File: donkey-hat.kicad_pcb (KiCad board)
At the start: 4 copper layers, 65 x 56.5 mm, 62 parts, among them J1 5V, J10 8, J11 9, J12 10, J13 11, J14 NEOPIXEL, J15 MPU-9250, J16 4, J17 5, J18 6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

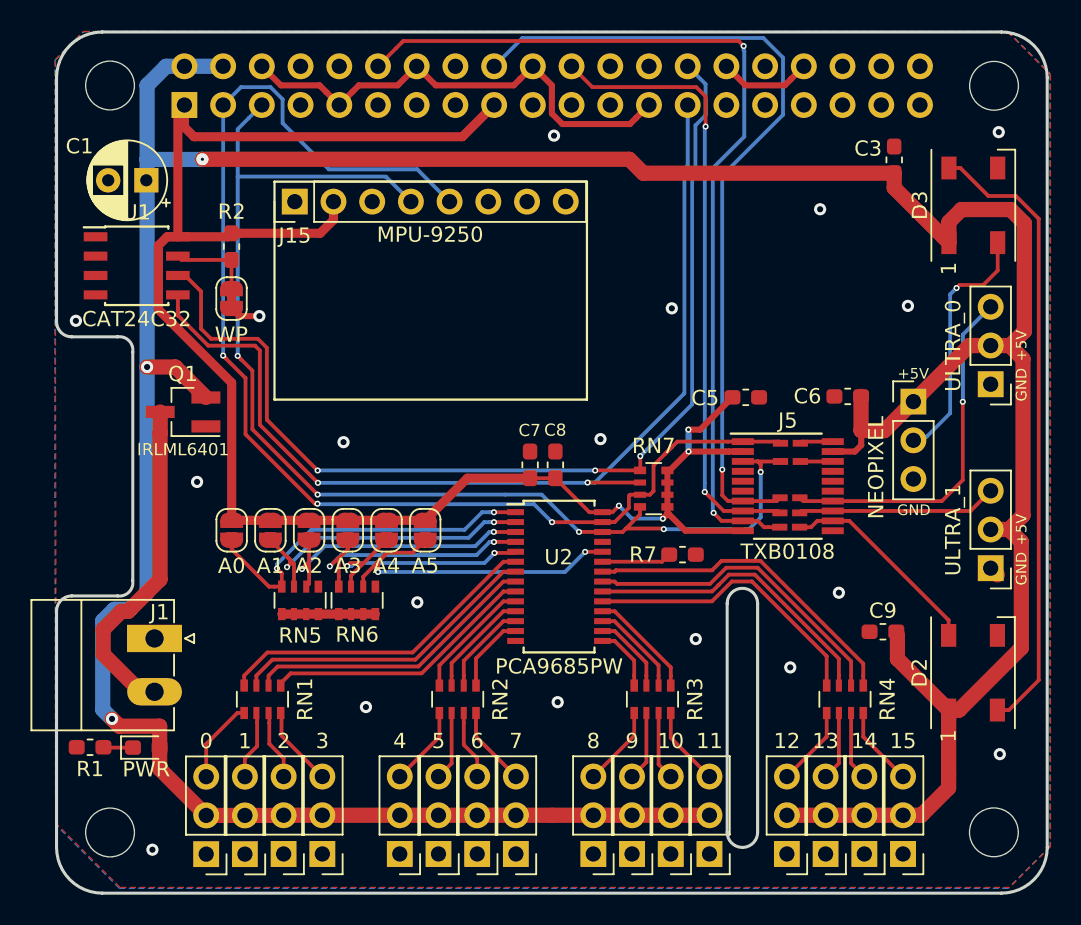
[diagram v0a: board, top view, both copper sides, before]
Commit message: Added logo and text.
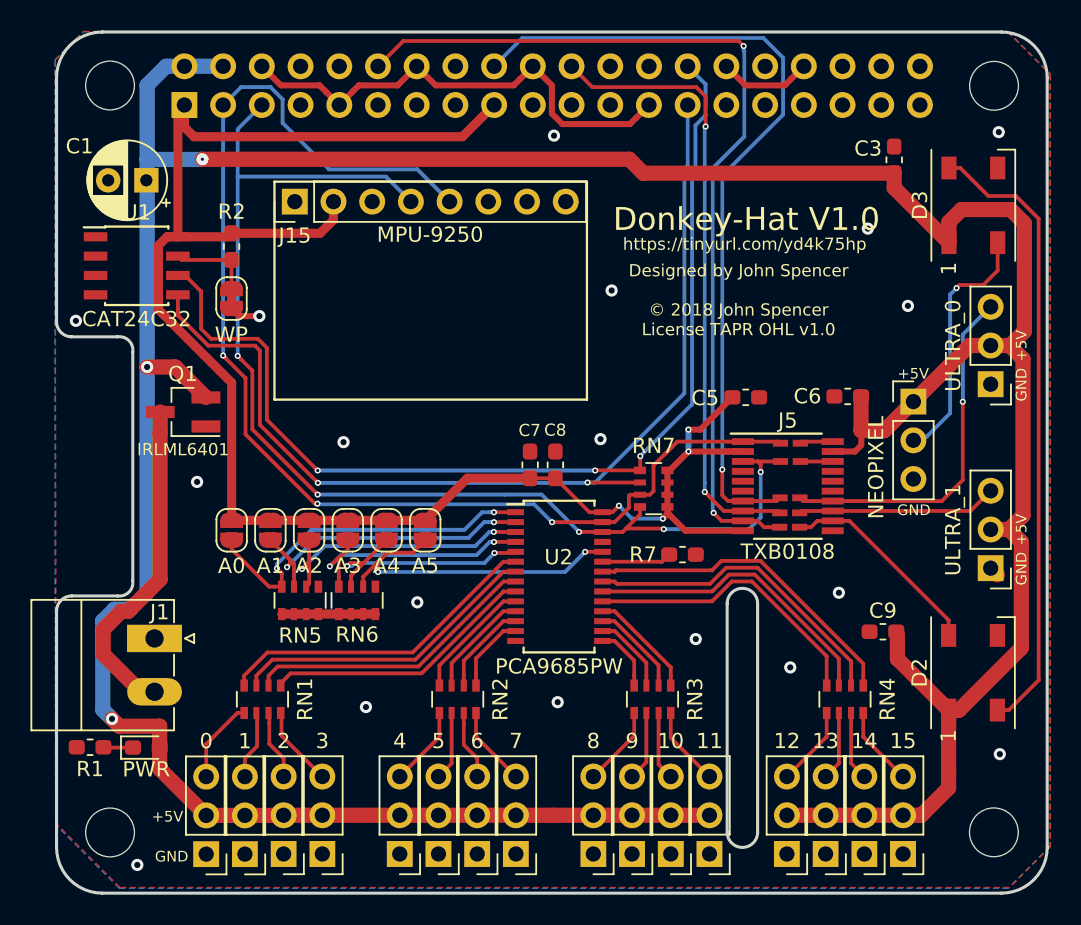
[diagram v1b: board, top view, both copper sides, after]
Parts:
- added G***: LOGO, libs:logo.HeartOfPluto, B.Cu at (91.5, 84.6)
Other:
- board text added: "Designed by John Spencer © 2018 John Spencer License TAPR OHL v1.0"
- board text added: "Donkey-Hat V1.0"
- board text added: "https://tinyurl.com/yd4k75hp"

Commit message: Schematic updated
PWM pins reduced.
level shifter removed.
Ultrasonic model changed.
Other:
- copper layers 4 -> 2
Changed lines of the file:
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@@
   (layers
     (0 F.Cu signal)
-    (1 In1.Cu signal)
-    (2 In2.Cu signal)
     (31 B.Cu signal)
     (32 B.Adhes user)
@@
     (40 Dwgs.User user)
     (41 Cmts.User user)
-    (42 Eco1.User user hide)
-    (43 Eco2.User user hide)
+    (42 Eco1.User user)
+    (43 Eco2.User user)
     (44 Edge.Cuts user)
     (45 Margin user)

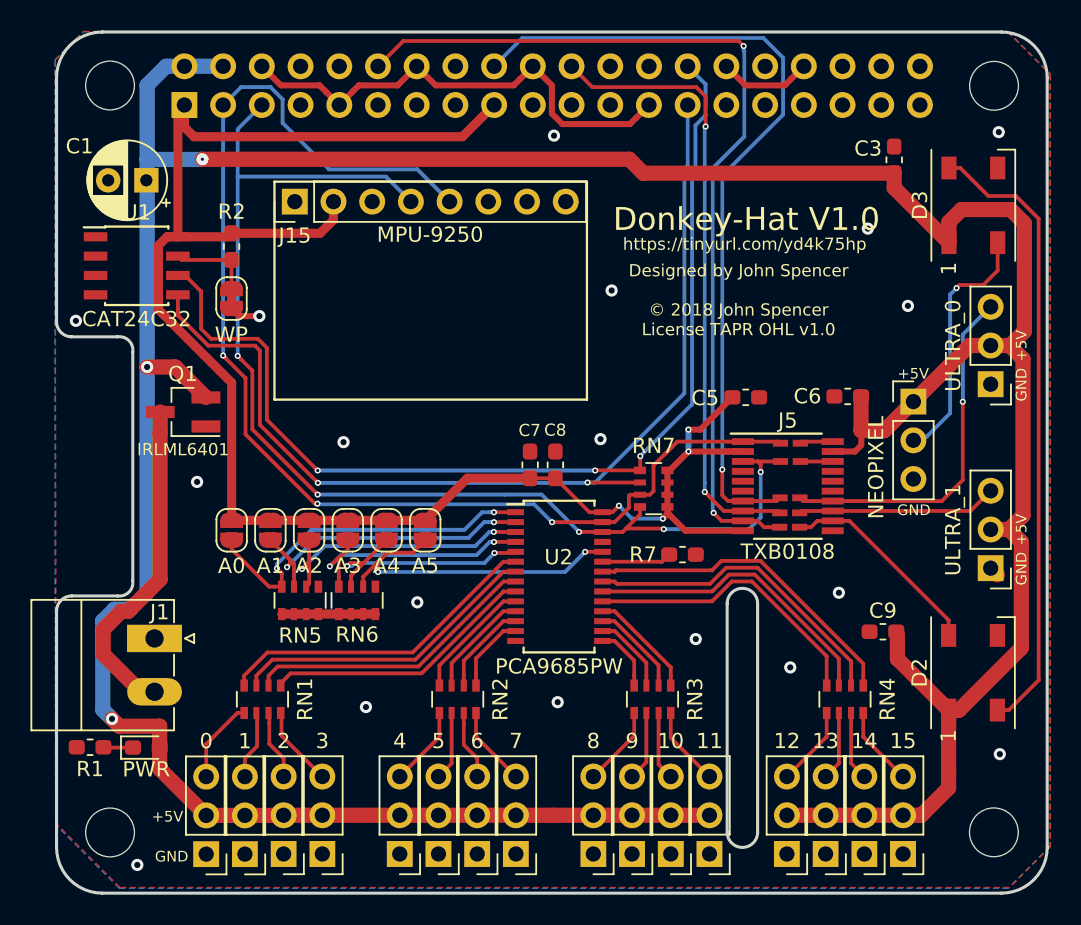
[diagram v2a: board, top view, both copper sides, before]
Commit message: New PCB to take in to account schematic changes
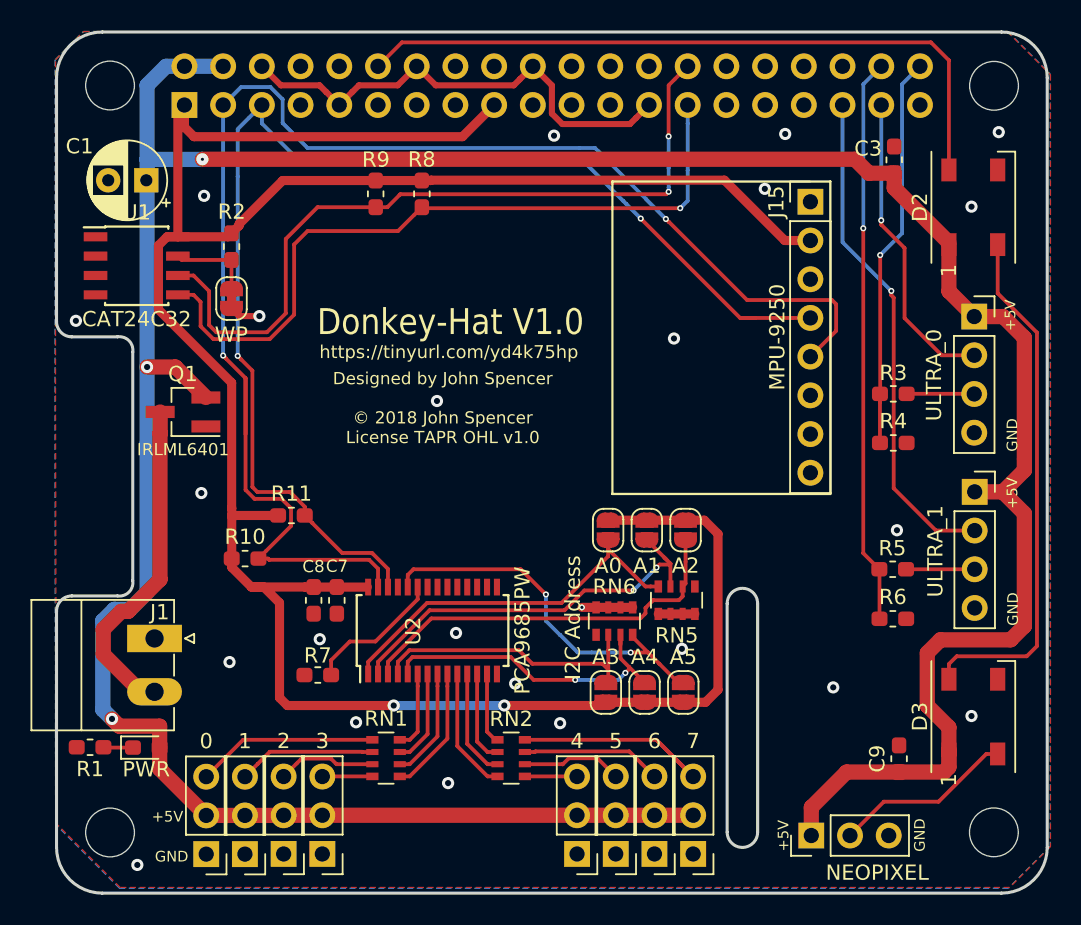
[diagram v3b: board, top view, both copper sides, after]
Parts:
- removed C5, C6: 100nF, Capacitor_SMD:C_0603_1608Metric_Pad1.05x0.95mm_HandSolder
- removed J10: 8, Connector_PinHeader_2.54mm:PinHeader_1x03_P2.54mm_Vertical
- removed J11: 9, Connector_PinHeader_2.54mm:PinHeader_1x03_P2.54mm_Vertical
- removed J12: 10, Connector_PinHeader_2.54mm:PinHeader_1x03_P2.54mm_Vertical
- removed J13: 11, Connector_PinHeader_2.54mm:PinHeader_1x03_P2.54mm_Vertical
- removed J20: 12, Connector_PinHeader_2.54mm:PinHeader_1x03_P2.54mm_Vertical
- removed J21: 13, Connector_PinHeader_2.54mm:PinHeader_1x03_P2.54mm_Vertical
- removed J22: 14, Connector_PinHeader_2.54mm:PinHeader_1x03_P2.54mm_Vertical
- removed J23: 15, Connector_PinHeader_2.54mm:PinHeader_1x03_P2.54mm_Vertical
- removed J5: TXB0108, Package_SO:TSSOP-20_4.4x6.5mm_P0.65mm
- removed JP11, JP12, JP13, JP8, JP9: LINK, libs:SolderJumper-2_small
- removed RN3, RN4: 220_Pack04, Resistor_SMD:R_Array_Convex_4x0603
- removed RN7: 3.9K_Pack04, Resistor_SMD:R_Array_Convex_4x0603
- added R10: 3.9K, Resistor_SMD:R_0603_1608Metric_Pad1.05x0.95mm_HandSolder, F.Cu at (90.9, 95.3)
- added R11: 3.9K, Resistor_SMD:R_0603_1608Metric_Pad1.05x0.95mm_HandSolder, F.Cu at (93.9, 92.5)
- added R3: 330, Resistor_SMD:R_0603_1608Metric_Pad1.05x0.95mm_HandSolder, F.Cu at (133.4, 84.5)
- added R4: 470, Resistor_SMD:R_0603_1608Metric_Pad1.05x0.95mm_HandSolder, F.Cu at (133.4, 87.8)
- added R5: 330, Resistor_SMD:R_0603_1608Metric_Pad1.05x0.95mm_HandSolder, F.Cu at (133.4, 96.0)
- added R6: 470, Resistor_SMD:R_0603_1608Metric_Pad1.05x0.95mm_HandSolder, F.Cu at (133.4, 99.3)
- added R8: 3.9K, Resistor_SMD:R_0603_1608Metric_Pad1.05x0.95mm_HandSolder, F.Cu at (102.5, 71.4)
- added R9: 3.9K, Resistor_SMD:R_0603_1608Metric_Pad1.05x0.95mm_HandSolder, F.Cu at (99.5, 71.4)
- C9: value 1uF -> 100nF
- J3, J4: footprint Connector_PinHeader_2.54mm:PinHeader_1x03_P2.54mm_Vertical -> Connector_PinSocket_2.54mm:PinSocket_1x04_P2.54mm_Vertical
- JP5: value A3 -> A5
- JP7: value A5 -> A3
- moved J15 33.8 mm to (128.0, 71.9), turned to 0 degrees
- moved D3 33.5 mm to (138.7, 105.7)
- moved D2 30.5 mm to (138.7, 72.3)
- moved J14 29.2 mm to (128.1, 113.5), turned to 90 degrees
- moved R7 25.2 mm to (95.7, 103.0), turned to 180 degrees
- moved JP2 24.7 mm to (114.7, 93.5)
- moved JP3 24.7 mm to (117.3, 93.5)
- moved JP4 24.7 mm to (119.8, 93.5)
- moved RN5 24.7 mm to (119.2, 98.1)
- moved JP5 24.4 mm to (119.7, 104.1), turned to 90 degrees
- moved JP6 20.0 mm to (117.1, 104.1), turned to 90 degrees
- moved C8 18.2 mm to (95.4, 98.1), turned to 270 degrees
- moved RN6 16.9 mm to (115.1, 99.5), turned to 90 degrees
- moved JP7 15.9 mm to (114.6, 104.1), turned to 90 degrees
- moved C7 15.5 mm to (96.9, 98.1), turned to 270 degrees
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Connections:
- D2 pad 4: /GPIO18_5 -> /GPIO18
- J3 pad 1: GND -> +5V
- J3 pad 2: +5V -> /GPIO26
- J3 pad 3: /GPIO24_5 -> Net-(J3-Pad3)
- J4 pad 1: GND -> +5V
- J4 pad 2: +5V -> /GPIO19
- J4 pad 3: /GPIO25_5 -> Net-(J4-Pad3)
- JP5 pad 2: /A3 -> /A5
- JP7 pad 2: /A5 -> /A3
- RN6 pad 2: /A5 -> /A3
- RN6 pad 4: /A3 -> /A5
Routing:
- net /GPIO24: track 54.7 -> 0.00 mm, vias 1 -> 0
- net +3V3: track 115.6 -> 169.7 mm, vias 4 -> 2
- net /GPIO25: track 41.1 -> 0.00 mm, vias 2 -> 0
- net /GPIO20: track 0.00 -> 37.2 mm, vias 0 -> 1
- net /GPIO19: track 0.00 -> 33.0 mm, vias 0 -> 1
- net +5V: track 237.1 -> 210.3 mm
- net /GPIO21: track 0.00 -> 25.8 mm, vias 0 -> 1
- net /GPIO24_5: track 23.5 -> 0.00 mm, vias 1 -> 0
- net /PWM15: track 21.8 -> 0.00 mm
- net /PWM14: track 21.0 -> 0.00 mm
- net /GPIO26: track 0.00 -> 20.2 mm, vias 0 -> 1
- net /PWM13: track 20.0 -> 0.00 mm
- net /PWM12: track 19.2 -> 0.00 mm
- net /EEDATA: track 67.0 -> 48.4 mm, vias 2 -> 1
- net /EECLK: track 68.6 -> 50.5 mm, vias 3 -> 2
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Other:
- board text added: "I2C Address"

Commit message: Added 5v regulator
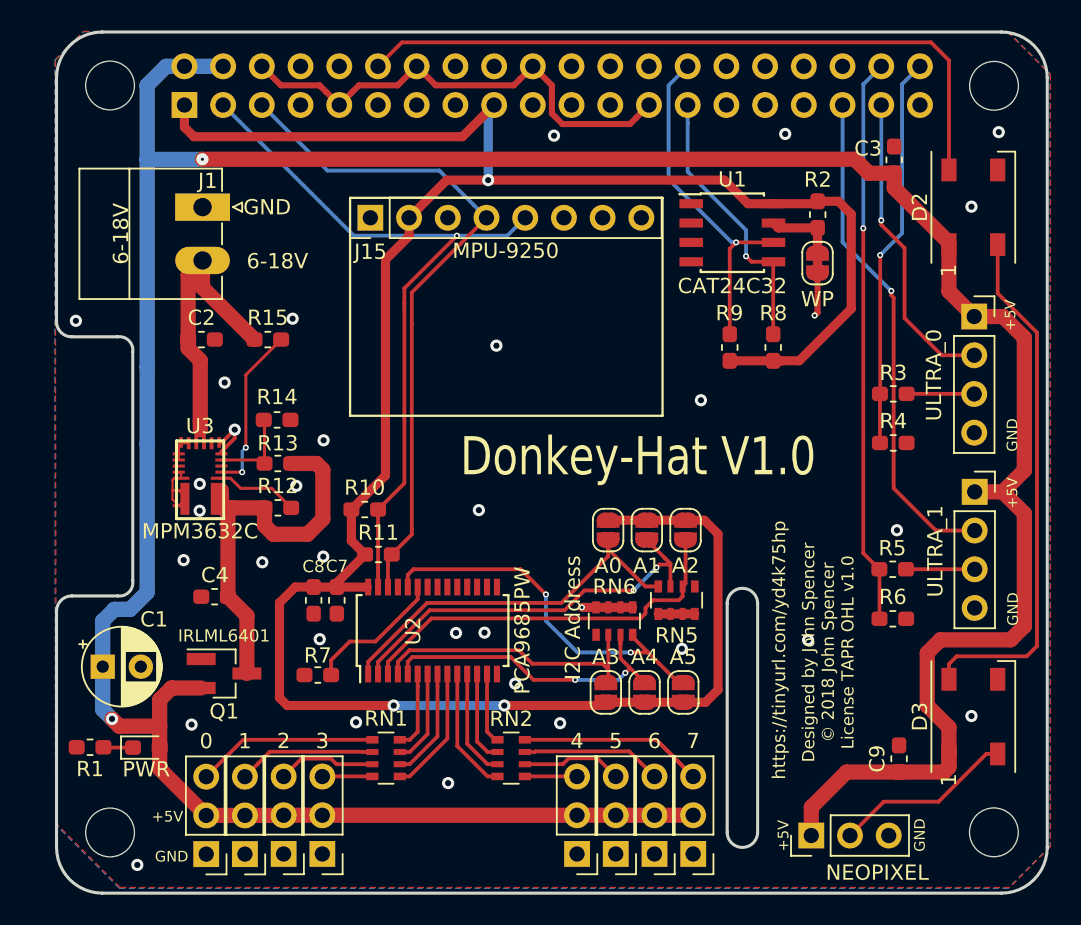
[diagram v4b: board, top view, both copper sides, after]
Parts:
- added C2: 10uF, Capacitor_SMD:C_0603_1608Metric_Pad1.05x0.95mm_HandSolder, F.Cu at (88.0, 81.0)
- added C4: 22uF, Capacitor_SMD:C_0603_1608Metric_Pad1.05x0.95mm_HandSolder, F.Cu at (88.9, 97.8)
- added R12: 1K, Resistor_SMD:R_0603_1608Metric_Pad1.05x0.95mm_HandSolder, F.Cu at (93.0, 92.0)
- added R13: 47K, Resistor_SMD:R_0603_1608Metric_Pad1.05x0.95mm_HandSolder, F.Cu at (93.0, 89.1)
- added R14: 8.87K, Resistor_SMD:R_0603_1608Metric_Pad1.05x0.95mm_HandSolder, F.Cu at (93.0, 86.2)
- added R15: 100K, Resistor_SMD:R_0603_1608Metric_Pad1.05x0.95mm_HandSolder, F.Cu at (92.4, 81.0)
- added U3: MPM3632C, libs:mpm3632c, F.Cu at (88.0, 90.2)
- J1: value 5V -> 6-18V
- moved U1 39.1 mm to (122.9, 74.0)
- moved JP1 38.5 mm to (128.5, 76.0)
- moved R2 38.5 mm to (128.5, 72.8)
- moved C1 32.0 mm to (81.6, 102.4), turned to 0 degrees
- moved J15 28.9 mm to (99.1, 73.0), turned to 90 degrees
- moved J1 28.5 mm to (88.1, 72.3)
- moved R9 25.3 mm to (122.7, 81.5), turned to 90 degrees
- moved R8 25.2 mm to (125.5, 81.5), turned to 90 degrees
- moved Q1 17.4 mm to (89.5, 102.9), turned to 0 degrees
- moved R10 8.48 mm to (98.8, 92.1)
- moved G*** 6.57 mm to (90.7, 89.7)
- moved R11 6.26 mm to (99.7, 95.1)
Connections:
- J1 pad 2: Net-(J1-Pad2) -> Net-(C2-Pad1)
- Q1 pad 3: Net-(J1-Pad2) -> Net-(C4-Pad1)
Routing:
- net /SDA_3.3: track 98.8 -> 49.1 mm, vias 2 -> 1
- net /SCL_3.3: track 82.3 -> 45.1 mm, vias 2 -> 0
- net /EEDATA: track 48.4 -> 18.2 mm
- net /EECLK: track 50.5 -> 22.7 mm, vias 2 -> 1
- net Net-(C4-Pad1): track 0.00 -> 26.5 mm
- net Net-(J1-Pad2): track 22.1 -> 0.00 mm
- net Net-(C2-Pad1): track 0.00 -> 21.5 mm
- net Net-(R15-Pad2): track 0.00 -> 11.1 mm, vias 0 -> 2
- net +3V3: track 169.7 -> 162.3 mm, vias 2 -> 3
- net GND: track 41.1 -> 47.0 mm, vias 24 -> 33
- net Net-(R13-Pad2): track 0.00 -> 5.80 mm
- net Net-(R12-Pad2): track 0.00 -> 5.53 mm
- net Net-(U3-Pad4): track 0.00 -> 4.67 mm
- net Net-(JP1-Pad1): track 5.51 -> 4.69 mm
- net +5V: track 210.3 -> 210.4 mm, vias 3 -> 2
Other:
- board text added: "6-18V"

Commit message: Updated to 0.3mm Vias.
Makes pcbway a lot cheaper to order from.
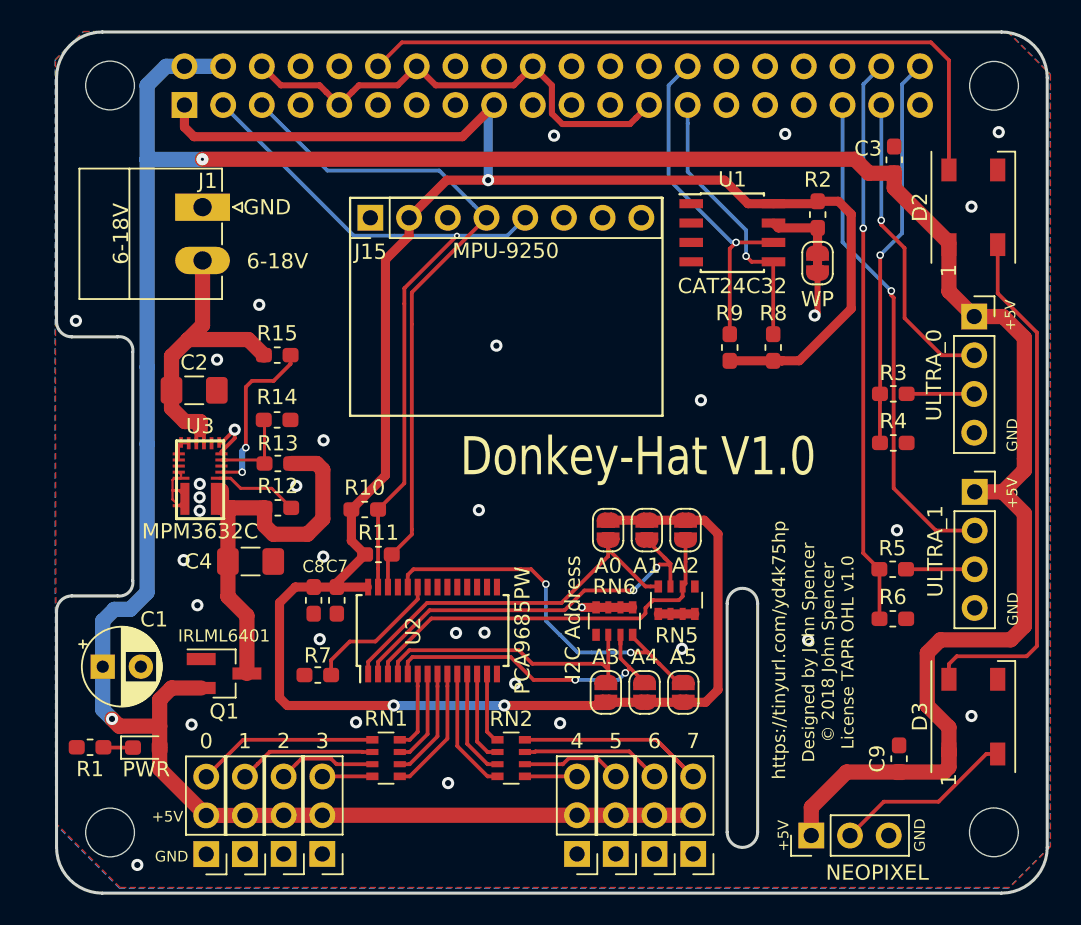
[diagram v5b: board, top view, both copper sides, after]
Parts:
- C2, C4: footprint Capacitor_SMD:C_0603_1608Metric_Pad1.05x0.95mm_HandSolder -> Capacitor_SMD:C_1206_3216Metric_Pad1.42x1.75mm_HandSolder
- moved C2 3.36 mm to (87.6, 84.3)
- moved C4 3.30 mm to (91.3, 95.5), turned to 0 degrees
- moved G*** 1.80 mm to (90.6, 87.9)
- moved R15 1.19 mm to (93.0, 82.0)
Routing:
- net GND: vias 33 -> 34
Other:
- net class Default: via_dia 0.4 -> 0.5; via_drill 0.2 -> 0.3

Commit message: Many via replacements later
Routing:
- net /SDA_3.3: track 49.1 -> 55.7 mm
